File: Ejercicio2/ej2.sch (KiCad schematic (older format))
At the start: 0 parts

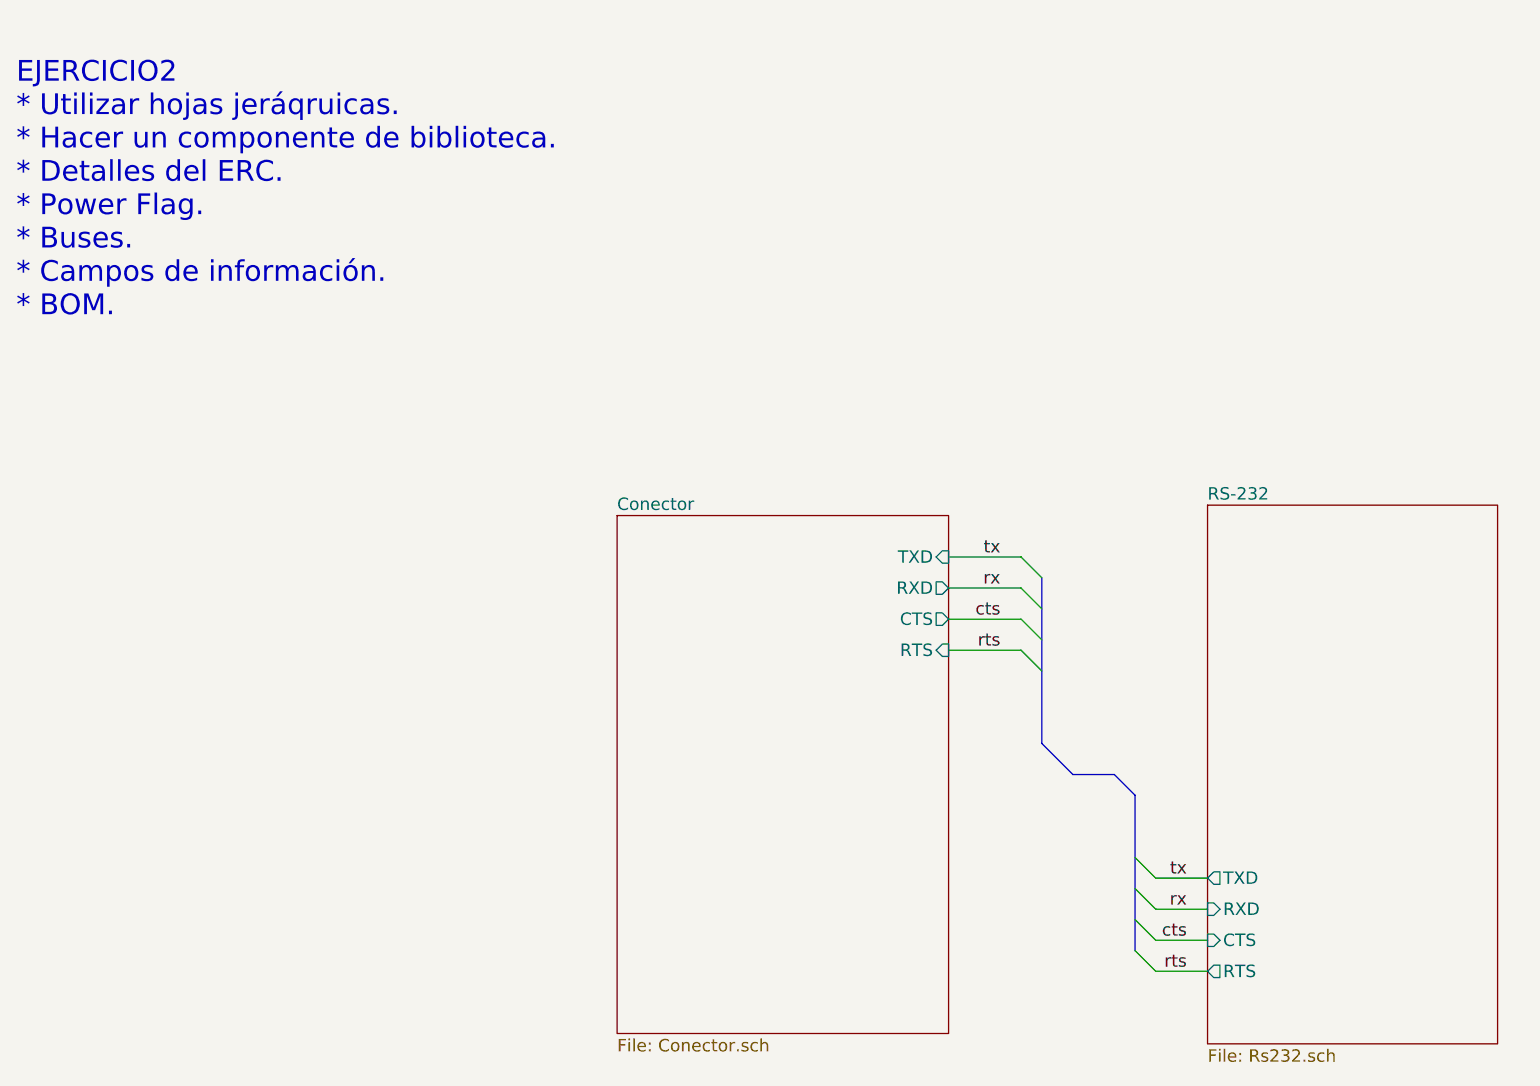
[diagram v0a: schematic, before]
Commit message: Agrego bus al esquemático. Quito resistor adicional.
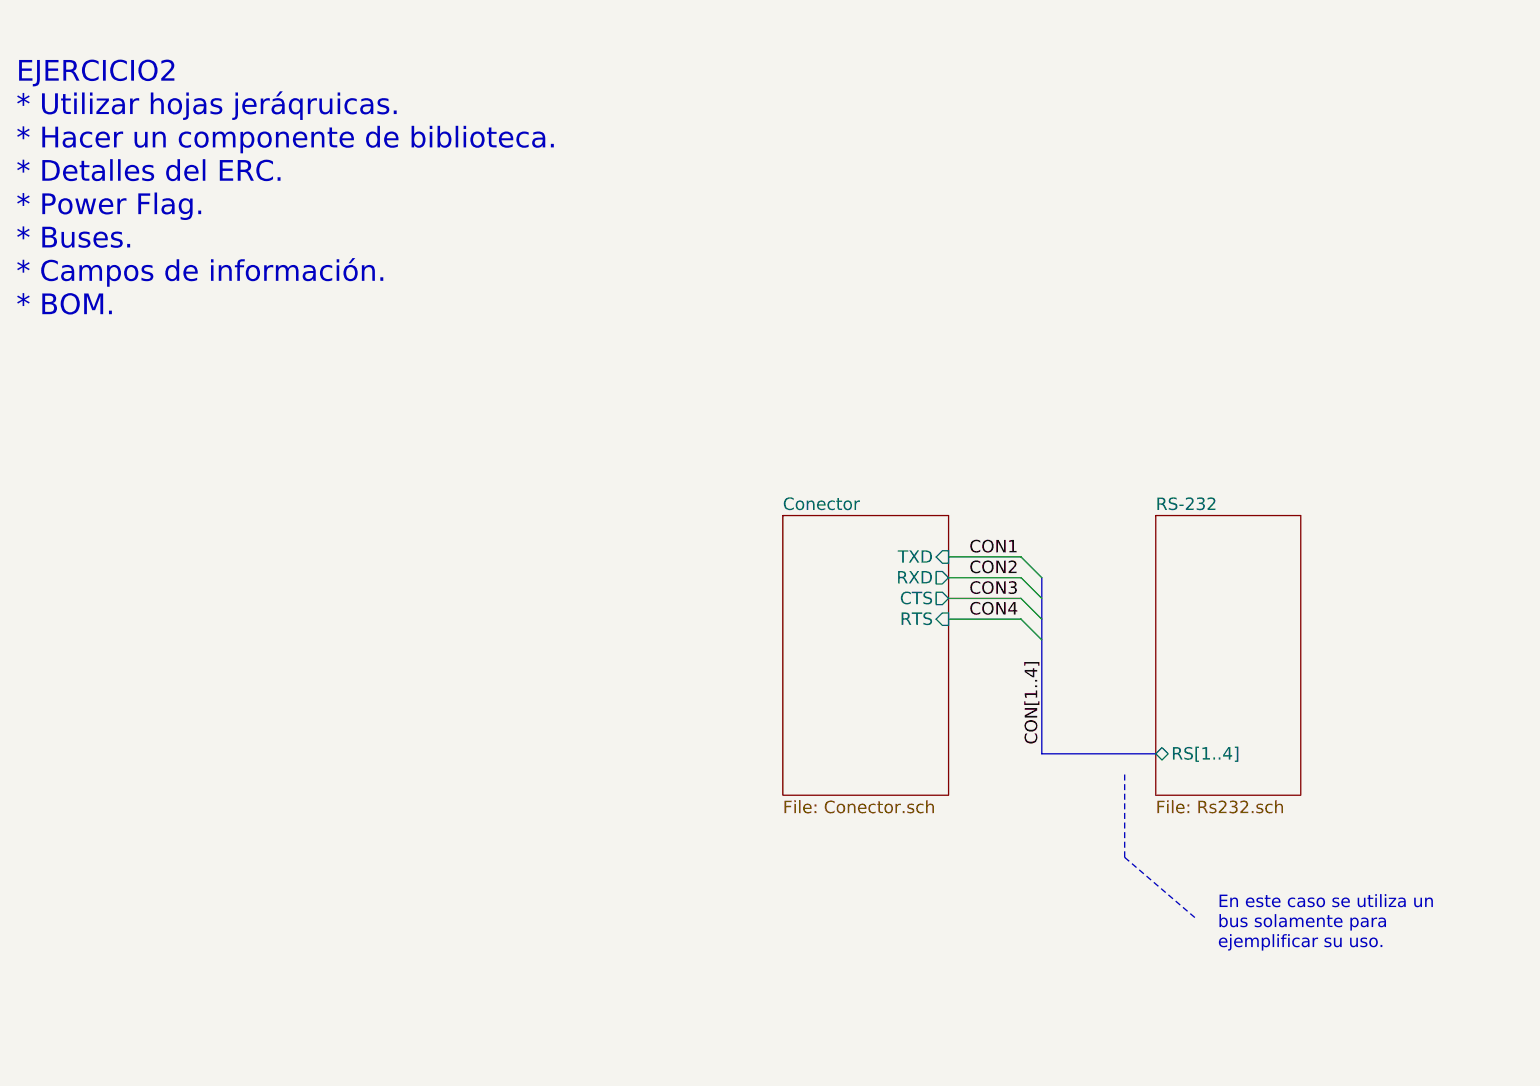
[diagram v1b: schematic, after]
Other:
- note added: "En este caso se utiliza un \nbus solamente para \nejemplificar su uso."
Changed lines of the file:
@@
 EESchema Schematic File Version 2
-LIBS:sp3232e
-LIBS:c
-LIBS:power
-LIBS:device
+LIBS:ej2
 LIBS:ej2-cache
 EELAYER 25 0
@@
 EJERCICIO2\n* Utilizar hojas jeráqruicas.\n* Hacer un componente de biblioteca.\n* Detalles del ERC.\n* Power Flag.\n* Buses.\n* Campos de información.\n* BOM.
 $Sheet
-S 3700 2900 1600 2500
+S 4500 2900 800  1350
 U 564E2838
 F0 "Conector" 60
 F1 "Conector.sch" 60
 F2 "TXD" I R 5300 3100 60
-F3 "RXD" O R 5300 3250 60
-F4 "RTS" I R 5300 3550 60
-F5 "CTS" O R 5300 3400 60
+F3 "RXD" O R 5300 3200 60
+F4 "RTS" I R 5300 3400 60
+F5 "CTS" O R 5300 3300 60
 $EndSheet
 $Sheet
-S 6550 2850 1400 2600
+S 6300 2900 700  1350
 U 564E3A27
 F0 "RS-232" 60
 F1 "Rs232.sch" 60
-F2 "TXD" O L 6550 4650 60
-F3 "RXD" I L 6550 4800 60
-F4 "CTS" I L 6550 4950 60
-F5 "RTS" O L 6550 5100 60
+F2 "RS[1..4]" B L 6300 4050 60
 $EndSheet
-Entry Wire Line
-	6200 4550 6300 4650
-Entry Wire Line
-	6200 4700 6300 4800
-Entry Wire Line
-	6200 4850 6300 4950
-Entry Wire Line
-	6200 5000 6300 5100
-Entry Wire Line
-	5650 3550 5750 3650
-Entry Wire Line
-	5650 3400 5750 3500
-Entry Wire Line
-	5650 3250 5750 3350
-Entry Wire Line
-	5650 3100 5750 3200
-Wire Bus Line
-	6200 4250 6200 5000
-Wire Bus Line
-	6200 4250 6100 4150
-Wire Bus Line
-	6100 4150 5900 4150
-Wire Bus Line
-	5900 4150 5750 4000
-Wire Bus Line
-	5750 4000 5750 3200
-Wire Wire Line
-	6300 4650 6550 4650
-Wire Wire Line
-	6550 4800 6300 4800
-Wire Wire Line
-	6550 5100 6300 5100
-Wire Wire Line
-	6550 4950 6300 4950
 Wire Wire Line
 	5650 3100 5300 3100
 Wire Wire Line
-	5650 3250 5300 3250
+	5650 3200 5300 3200
+Wire Wire Line
+	5650 3300 5300 3300
 Wire Wire Line
 	5650 3400 5300 3400
-Wire Wire Line
-	5650 3550 5300 3550
-Text Label 5550 3250 2    60   ~ 0
-rx
-Text Label 5550 3100 2    60   ~ 0
-tx
-Text Label 5550 3400 2    60   ~ 0
-cts
-Text Label 5550 3550 2    60   ~ 0
-rts
-Text Label 6450 4800 2    60   ~ 0
-rx
-Text Label 6450 4650 2    60   ~ 0
-tx
-Text Label 6450 4950 2    60   ~ 0
-cts
-Text Label 6450 5100 2    60   ~ 0
-rts
+Text Label 5400 3100 0    60   ~ 0
+CON1
+Text Label 5400 3200 0    60   ~ 0
+CON2
+Text Label 5400 3300 0    60   ~ 0
+CON3
+Text Label 5400 3400 0    60   ~ 0
+CON4
+Entry Wire Line
+	5650 3100 5750 3200
+Entry Wire Line
+	5650 3200 5750 3300
+Entry Wire Line
+	5650 3300 5750 3400
+Entry Wire Line
+	5650 3400 5750 3500
+Wire Bus Line
+	5750 3200 5750 4050
+Wire Bus Line
+	5750 4050 6300 4050
+Wire Notes Line
+	6150 4150 6150 4550
+Wire Notes Line
+	6150 4550 6500 4850
+Text Notes 6600 5000 0    60   ~ 0
+En este caso se utiliza un \nbus solamente para \nejemplificar su uso.
+Text Label 5750 3600 3    60   ~ 0
+CON[1..4]
 $EndSCHEMATC

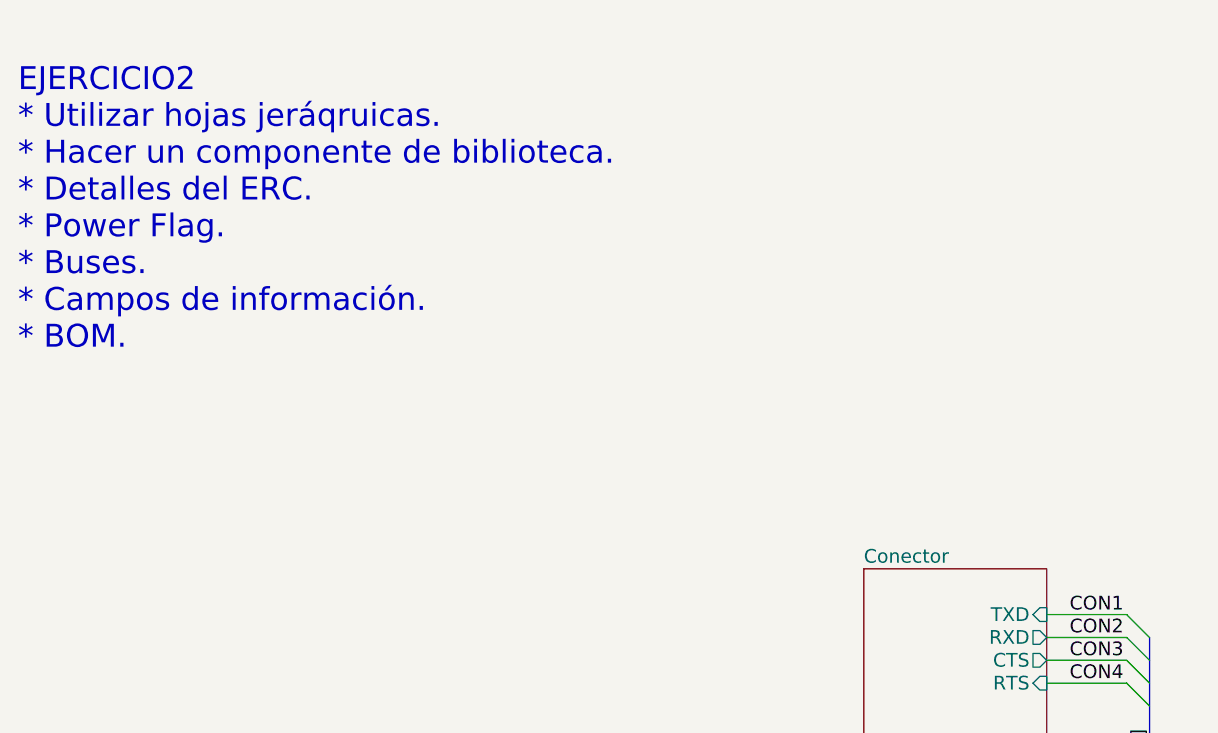
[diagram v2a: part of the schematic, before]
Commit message: Versión del Ejercicio2 con CAN.
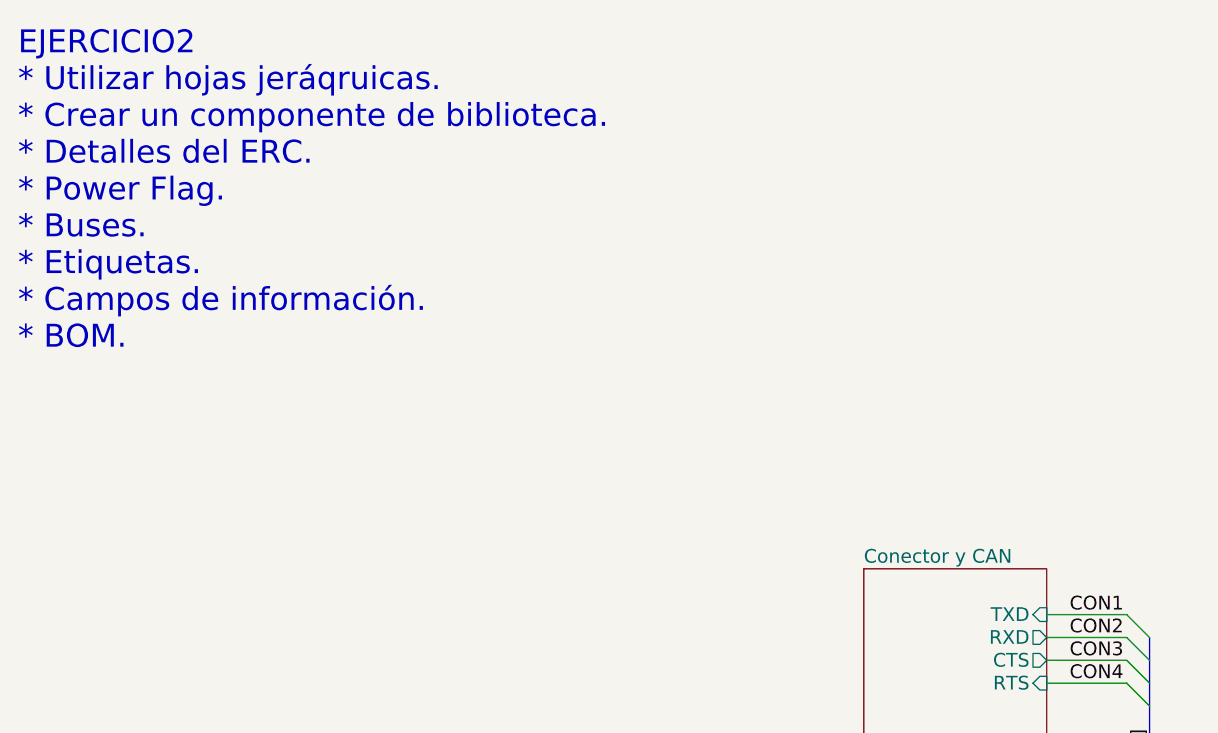
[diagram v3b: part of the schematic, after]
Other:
- note added: "EJERCICIO2\n* Utilizar hojas jeráqruicas.\n* Crear un componente de biblioteca.\n* Detalles del ERC.\n* Power Flag.\n* Buses.\n* Etiquetas.\n* Campos de información.\n* BOM."
- note removed: "EJERCICIO2\n* Utilizar hojas jeráqruicas.\n* Hacer un componente de biblioteca.\n* Detalles del ERC.\n* Power Flag.\n* Buses.\n* Campos de información.\n* BOM."
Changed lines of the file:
@@
 LIBS:ej2
 LIBS:power
-LIBS:ej2-cache
 EELAYER 25 0
 EELAYER END
@@
 encoding utf-8
 Sheet 1 3
-Title "Ejercicio 2 - Curso Kicad"
-Date "2015-11-19"
+Title "Ejercicio 2 - Curso Kicad - principal"
+Date "2015-11-26"
 Rev "1.0"
 Comp "Instituto Nacional de Tecnología Industrial INTI-CMNB"
-Comment1 ""
+Comment1 "Autores: D. Alamon, D. Brengi, N. Scotti"
 Comment2 ""
 Comment3 ""
@@
 $EndDescr
 Text Notes 800  1950 0    100  ~ 0
-EJERCICIO2\n* Utilizar hojas jeráqruicas.\n* Hacer un componente de biblioteca.\n* Detalles del ERC.\n* Power Flag.\n* Buses.\n* Campos de información.\n* BOM.
+EJERCICIO2\n* Utilizar hojas jeráqruicas.\n* Crear un componente de biblioteca.\n* Detalles del ERC.\n* Power Flag.\n* Buses.\n* Etiquetas.\n* Campos de información.\n* BOM.
 $Sheet
 S 4500 2900 800  1350
 U 564E2838
-F0 "Conector" 60
+F0 "Conector y CAN" 60
 F1 "Conector.sch" 60
 F2 "TXD" I R 5300 3100 60
